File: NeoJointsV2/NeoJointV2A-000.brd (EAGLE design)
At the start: 11 x 22.9 mm, 6 parts

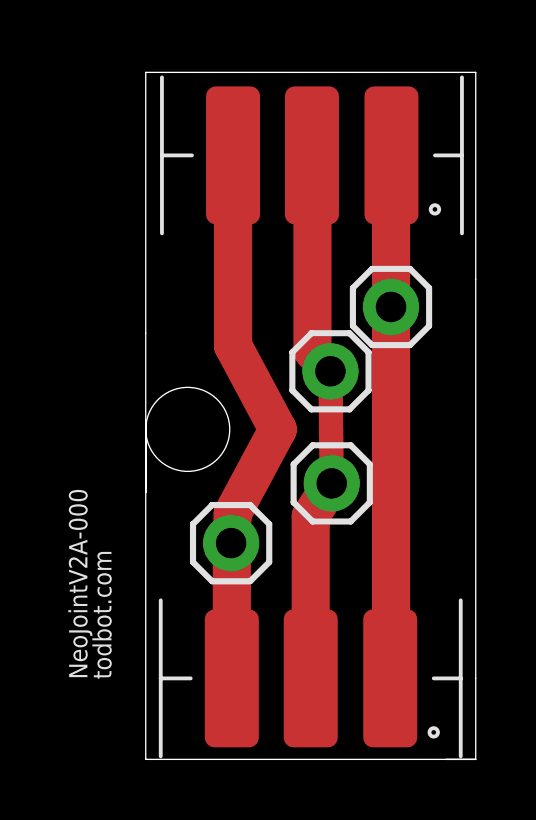
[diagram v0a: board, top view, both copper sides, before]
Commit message: layout fixes for 000,090,120
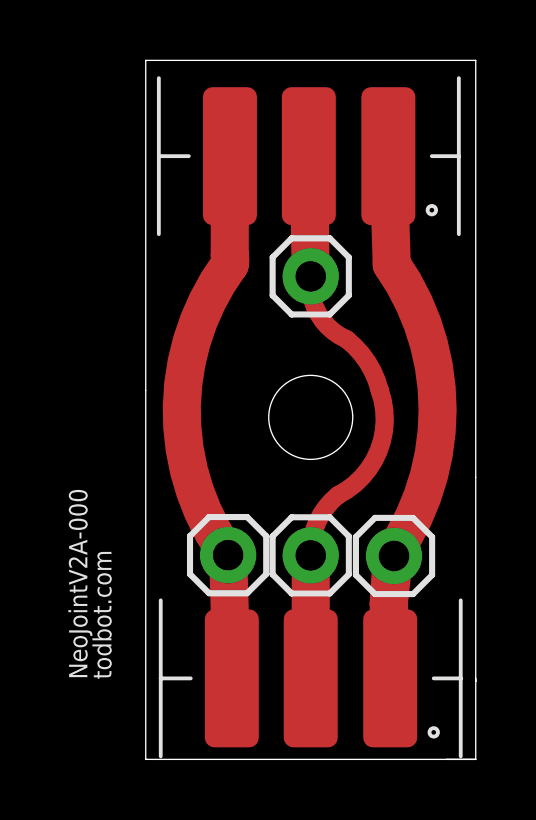
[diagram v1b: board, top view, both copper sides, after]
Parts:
- moved JP1 8.30 mm to (8.28, 6.78)
- moved JP2 3.23 mm to (5.50, 16.1)
- moved JP4 2.50 mm to (5.50, 6.80)
- moved JP3 0.41 mm to (2.75, 6.81)
- moved U$2 0.11 mm to (5.44, 20.1)
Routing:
- net A: track 17.4 -> 19.0 mm
- net C: track 18.3 -> 17.5 mm
- net B: track 17.9 -> 18.5 mm
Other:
- board size 11 x 22.9 mm -> 11 x 23.3 mm
